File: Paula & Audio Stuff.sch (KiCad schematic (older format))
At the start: 35 parts, among them CN1 LEFT_JOY, CN2 RIGHT_JOY, U15 74LS157, U3 PAULA

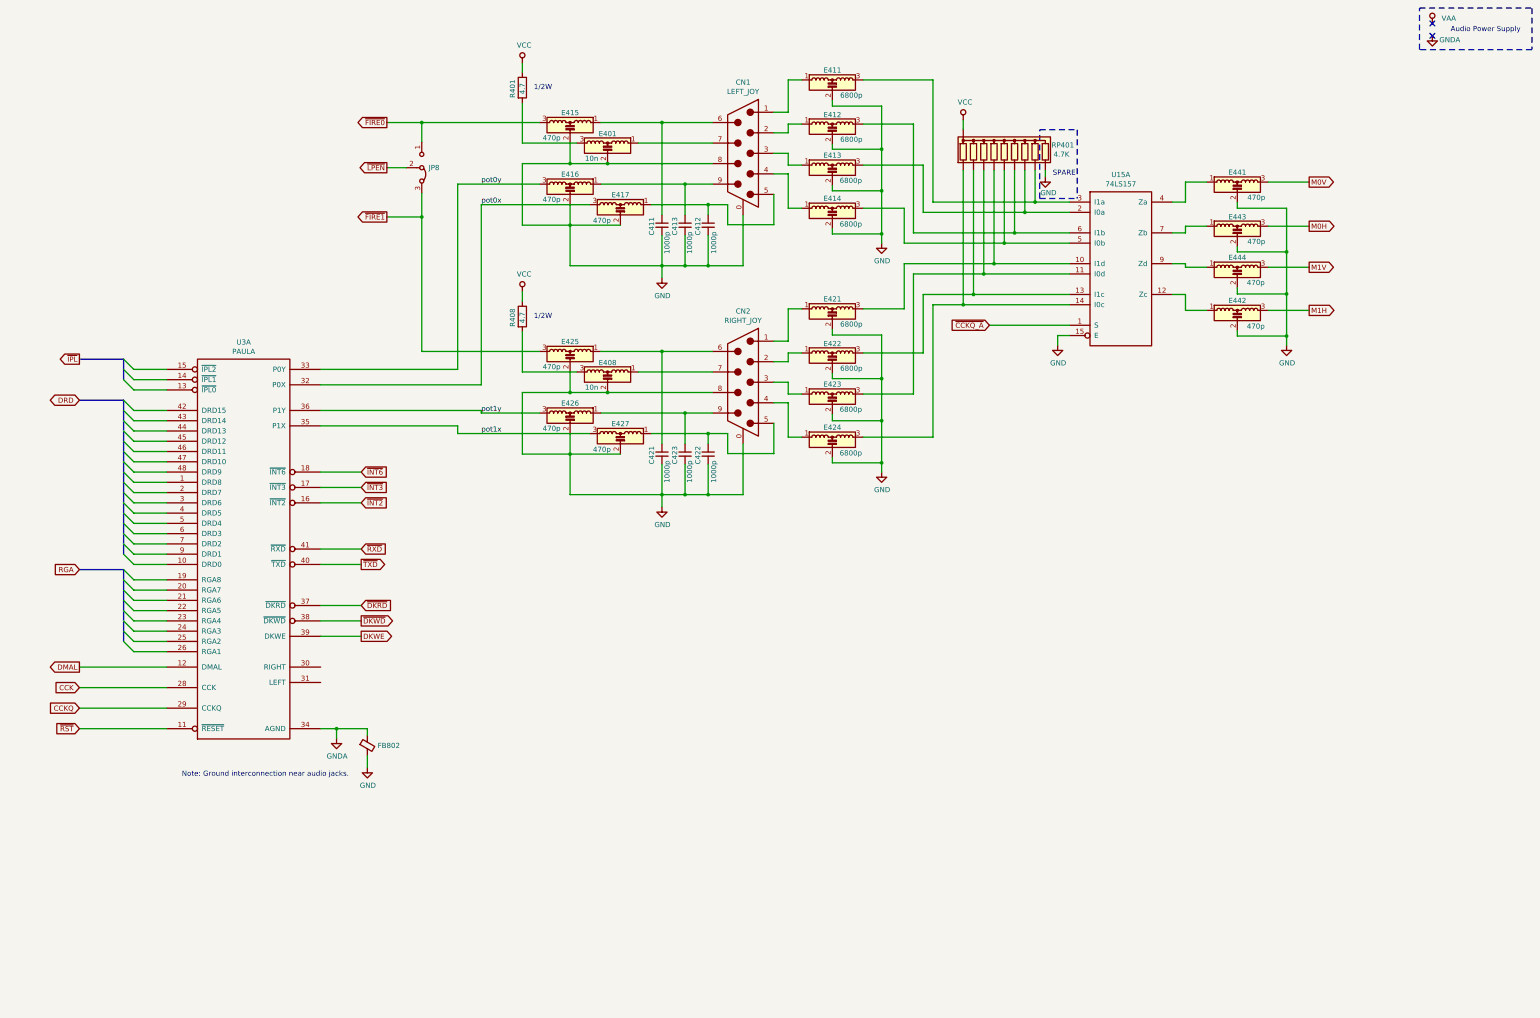
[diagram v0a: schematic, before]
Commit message: Add audio filters
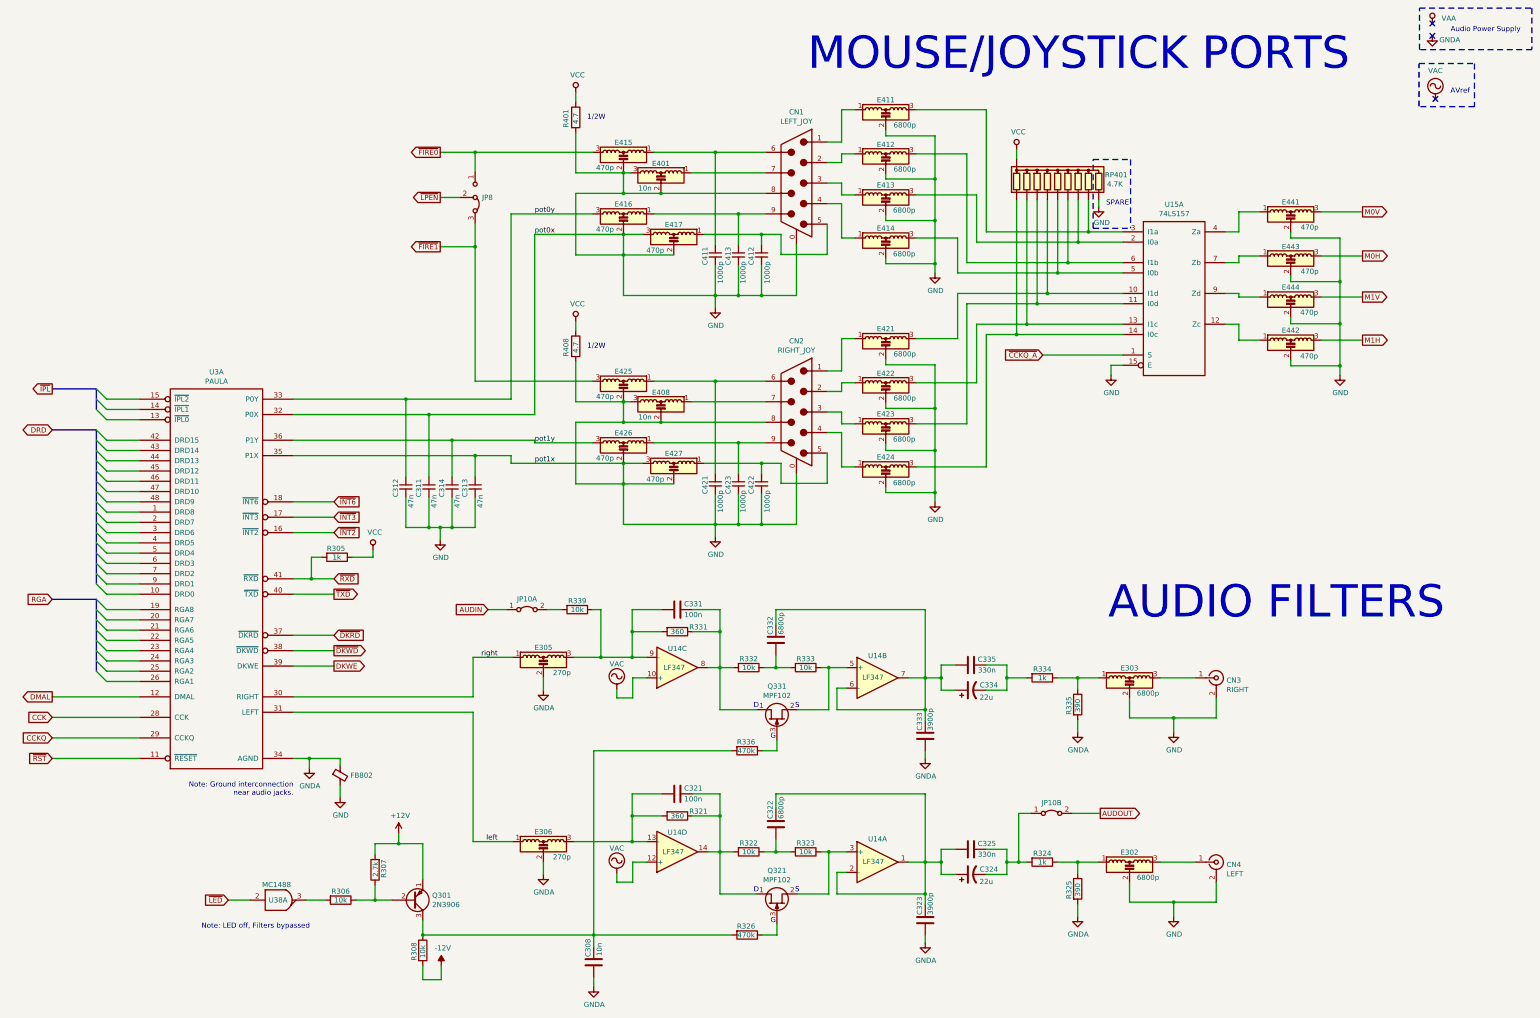
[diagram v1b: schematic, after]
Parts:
- added C308: 10n, symbol Device:C
- added C311, C312, C313, C314: 47n, symbol Device:C_Small
- added C321, C331: 100n, symbol Device:C
- added C322, C332: 6800p, symbol Device:C
- added C323, C333: 3900p, symbol Device:C
- added C324, C334: 22u, symbol Device:CP1
- added C325, C335: 330n, symbol Device:C
- added CN3: RIGHT, symbol Connector:Conn_Coaxial
- added CN4: LEFT, symbol Connector:Conn_Coaxial
- added E302, E303: 6800p, symbol Device:EMI_Filter_LCL
- added E305, E306: 270p, symbol Device:EMI_Filter_LCL
- added JP10A, JP10B: Jumper_2_Bridged, symbol Jumper:Jumper_2_Bridged
- added Q301: 2N3906, symbol Device:Q_PNP_EBC
- added Q321, Q331: MPF102, symbol Device:Q_NJFET_DSG
- added R305, R324, R334: 1k, symbol Device:R
- added R306, R308, R322, R323, R332, R333, R339: 10k, symbol Device:R
- added R307: 2.7k, symbol Device:R
- added R321, R331: 360, symbol Device:R
- added R325, R335: 390, symbol Device:R
- added R326, R336: 470k, symbol Device:R
- added U14: LF347, symbol Amplifier_Operational:TL084
- added U38: MC1488, MODULE, symbol MC1488:MC1488
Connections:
- net pot0x is gone; now on net GND: E417.3, U3.32 (P0X)
- net pot1x is gone; now on net GND: E427.3, U3.35 (P1X)
- net GND: now also E401.3, E408.3, R401.2, R408.2, C311.1, C311.2, C312.2, C313.1, C313.2, C314.2, CN3.2 (Ext), CN4.2 (Ext), E302.2, E303.2
- net GNDA: now also C308.2, C323.2, C333.2, E305.2, E306.2, R325.2, R335.2
- net VCC: now also R305.1
- net pot0y: now also C312.1
- net pot1y: now also C314.1
- net ~RXD: now also R305.2
- net right: now reaches U3.30 (RIGHT)
- net right: now also E305.1
- net left: now reaches U3.31 (LEFT)
- net left: now also E306.1
- new net: C322.1, C323.1, C324.1, C325.2, U14.1, U14.2 (-)
- new net: Q321.2 (S), R323.1, U14.3 (+)
- new net: Q331.2 (S), R333.1, U14.5 (+)
- new net: C332.1, C333.1, C334.1, C335.2, U14.6 (-), U14.7
- new net: C331.1, Q331.1 (D), R331.1, R332.2, U14.8
- new net: C331.2, E305.3, R331.2, R339.1, U14.9 (-)
- new net: C321.2, E306.3, R321.2, U14.13 (-)
- new net: C321.1, Q321.1 (D), R321.1, R322.2, U14.14
- new net: C322.2, R322.1, R323.2
- new net: C324.2, C325.1, JP10B.1 (A), R324.2
- new net: E302.1, R324.1, R325.1
- new net: CN4.1 (In), E302.3
- new net: Q321.3 (G), R326.1
- new net: C308.1, Q301.3 (C), R308.1, R326.2, R336.2
- new net: C332.2, R332.1, R333.2
- new net: C334.2, C335.1, R334.2
- new net: E303.1, R334.1, R335.1
- new net: CN3.1 (In), E303.3
- new net: Q331.3 (G), R336.1
- new net: Q301.2 (B), R306.1, R307.1
- new net: R306.2, U38.3
- new net: JP10A.2 (B), R339.2
- new net +12V: Q301.1 (E), R307.2
- new net -12V: R308.2
- new net AUDIN: JP10A.1 (A)
- new net AUDOUT: JP10B.2 (B)
- new net VAC: U14.10 (+), U14.12 (+)
- new net ~LED: U38.2
- no-connect marks 2 -> 3
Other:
- note added: "AUDIO FILTERS"
- note added: "AVref"
- note added: "D"
- note added: "G"
- note added: "MOUSE/JOYSTICK PORTS"
- note added: "Note: Ground interconnection\nnear audio jacks."
- note added: "Note: LED off, Filters bypassed"
- note added: "S"
- note removed: "Note: Ground interconnection near audio jacks."
- moved on the sheet: C411, C412, C413, C421, C422, C423, CN1, CN2, E401, E408, E411, E412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
